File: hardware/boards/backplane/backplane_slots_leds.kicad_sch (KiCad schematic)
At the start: 18 parts, among them J1 DC_IN_SCREW_TERMINAL, J10 I2C_CHAIN_IN, J11 I2C_CHAIN_OUT, J12 LED_EXT_OUT, J2 XT30U(2+2)-F.G.B_SLOT1, J3 XT30U(2+2)-F.G.B_SLOT2, J4 XT30U(2+2)-F.G.B_SLOT3, J5 XT30U(2+2)-F.G.B_SLOT4, J6 XT30U(2+2)-F.G.B_SLOT5, J7 XT30U(2+2)-F.G.B_SLOT6, J8 LED_EXT_IN, J9 DC_CHAIN_OUT

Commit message: Rename XT30U footprint
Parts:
- J2, J3, J4, J5, J6, J7: footprint mini-rack-power:Amass_XT30U_2plus2_F_RightAngle_Mechanical -> mini-rack-power:Amass_XT30U_2plus2_F
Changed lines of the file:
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@@
 			)
 		)
-		(property "Footprint" "mini-rack-power:Amass_XT30U_2plus2_F_RightAngle_Mechanical"
+		(property "Footprint" "mini-rack-power:Amass_XT30U_2plus2_F"
 			(at 92.71 33.02 0)
 			(hide yes)
@@
 			)
 		)
-		(property "Description" "Amass XT30U 2+2 female slot connector; female PCB land pattern needs verification"
+		(property "Description" "Amass XT30U 2+2 female vertical/180-degree slot connector"
 			(at 92.71 33.02 0)
 			(hide yes)
@@
 			)
 		)
-		(property "Footprint" "mini-rack-power:Amass_XT30U_2plus2_F_RightAngle_Mechanical"
+		(property "Footprint" "mini-rack-power:Amass_XT30U_2plus2_F"
 			(at 92.71 55.88 0)
 			(hide yes)
@@
 			)
 		)
-		(property "Description" "Amass XT30U 2+2 female slot connector; female PCB land pattern needs verification"
+		(property "Description" "Amass XT30U 2+2 female vertical/180-degree slot connector"
 			(at 92.71 55.88 0)
 			(hide yes)
@@
 			)
 		)
-		(property "Footprint" "mini-rack-power:Amass_XT30U_2plus2_F_RightAngle_Mechanical"
+		(property "Footprint" "mini-rack-power:Amass_XT30U_2plus2_F"
 			(at 92.71 78.74 0)
 			(hide yes)
@@
 			)
 		)
-		(property "Description" "Amass XT30U 2+2 female slot connector; female PCB land pattern needs verification"
+		(property "Description" "Amass XT30U 2+2 female vertical/180-degree slot connector"
 			(at 92.71 78.74 0)
 			(hide yes)
@@
 			)
 		)
-		(property "Footprint" "mini-rack-power:Amass_XT30U_2plus2_F_RightAngle_Mechanical"
+		(property "Footprint" "mini-rack-power:Amass_XT30U_2plus2_F"
 			(at 151.13 33.02 0)
 			(hide yes)
@@
 			)
 		)
-		(property "Description" "Amass XT30U 2+2 female slot connector; female PCB land pattern needs verification"
+		(property "Description" "Amass XT30U 2+2 female vertical/180-degree slot connector"
 			(at 151.13 33.02 0)
 			(hide yes)
@@
 			)
 		)
-		(property "Footprint" "mini-rack-power:Amass_XT30U_2plus2_F_RightAngle_Mechanical"
+		(property "Footprint" "mini-rack-power:Amass_XT30U_2plus2_F"
 			(at 151.13 55.88 0)
 			(hide yes)
@@
 			)
 		)
-		(property "Description" "Amass XT30U 2+2 female slot connector; female PCB land pattern needs verification"
+		(property "Description" "Amass XT30U 2+2 female vertical/180-degree slot connector"
 			(at 151.13 55.88 0)
 			(hide yes)
@@
 			)
 		)
-		(property "Footprint" "mini-rack-power:Amass_XT30U_2plus2_F_RightAngle_Mechanical"
+		(property "Footprint" "mini-rack-power:Amass_XT30U_2plus2_F"
 			(at 151.13 78.74 0)
 			(hide yes)
@@
 			)
 		)
-		(property "Description" "Amass XT30U 2+2 female slot connector; female PCB land pattern needs verification"
+		(property "Description" "Amass XT30U 2+2 female vertical/180-degree slot connector"
 			(at 151.13 78.74 0)
 			(hide yes)

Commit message: Update board layouts and add SW3538 datasheet
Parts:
- added J14: LED_EXT_IN, Connector_PinHeader_2.54mm:PinHeader_1x03_P2.54mm_Vertical, symbol Connector_Generic:Conn_01x03
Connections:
- net DC_IN+: now also J1.2 (Pin_2); no longer J1.1 (Pin_1)
- net GND: now also J1.1 (Pin_1), J8.1 (Pin_1); no longer D2.3 (VSS), D3.3 (VSS), D4.3 (VSS), D5.3 (VSS), D6.3 (VSS), J1.2 (Pin_2), J8.3 (Pin_3)
- net I2C_UP_SCL: now also J10.2 (Pin_2), J11.2 (Pin_2); no longer J10.3 (Pin_3), J11.3 (Pin_3)
- net I2C_UP_SDA: now also J10.3 (Pin_3), J11.3 (Pin_3); no longer J10.2 (Pin_2), J11.2 (Pin_2)
- net LED_VDD: no longer J8.1 (Pin_1)
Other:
- moved on the sheet: D1, D2, D3, D4, D5, D6, J1, J10, J11, J8

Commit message: Starrting to move things around
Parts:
- removed J2: XT30U(2+2)-F.G.B_SLOT1, mini-rack-power:Amass_XT30U_2plus2_F, symbol Connector_Generic:Conn_01x04
- removed J3: XT30U(2+2)-F.G.B_SLOT2, mini-rack-power:Amass_XT30U_2plus2_F, symbol Connector_Generic:Conn_01x04
- removed J4: XT30U(2+2)-F.G.B_SLOT3, mini-rack-power:Amass_XT30U_2plus2_F, symbol Connector_Generic:Conn_01x04
- removed J5: XT30U(2+2)-F.G.B_SLOT4, mini-rack-power:Amass_XT30U_2plus2_F, symbol Connector_Generic:Conn_01x04
- removed J6: XT30U(2+2)-F.G.B_SLOT5, mini-rack-power:Amass_XT30U_2plus2_F, symbol Connector_Generic:Conn_01x04
- removed J7: XT30U(2+2)-F.G.B_SLOT6, mini-rack-power:Amass_XT30U_2plus2_F, symbol Connector_Generic:Conn_01x04
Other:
- note removed: "XT30 pin assumption: 1=DC_IN+, 2=GND, 3=SDA, 4=SCL. Verify XT30U female electrical footprint before PCB layout."

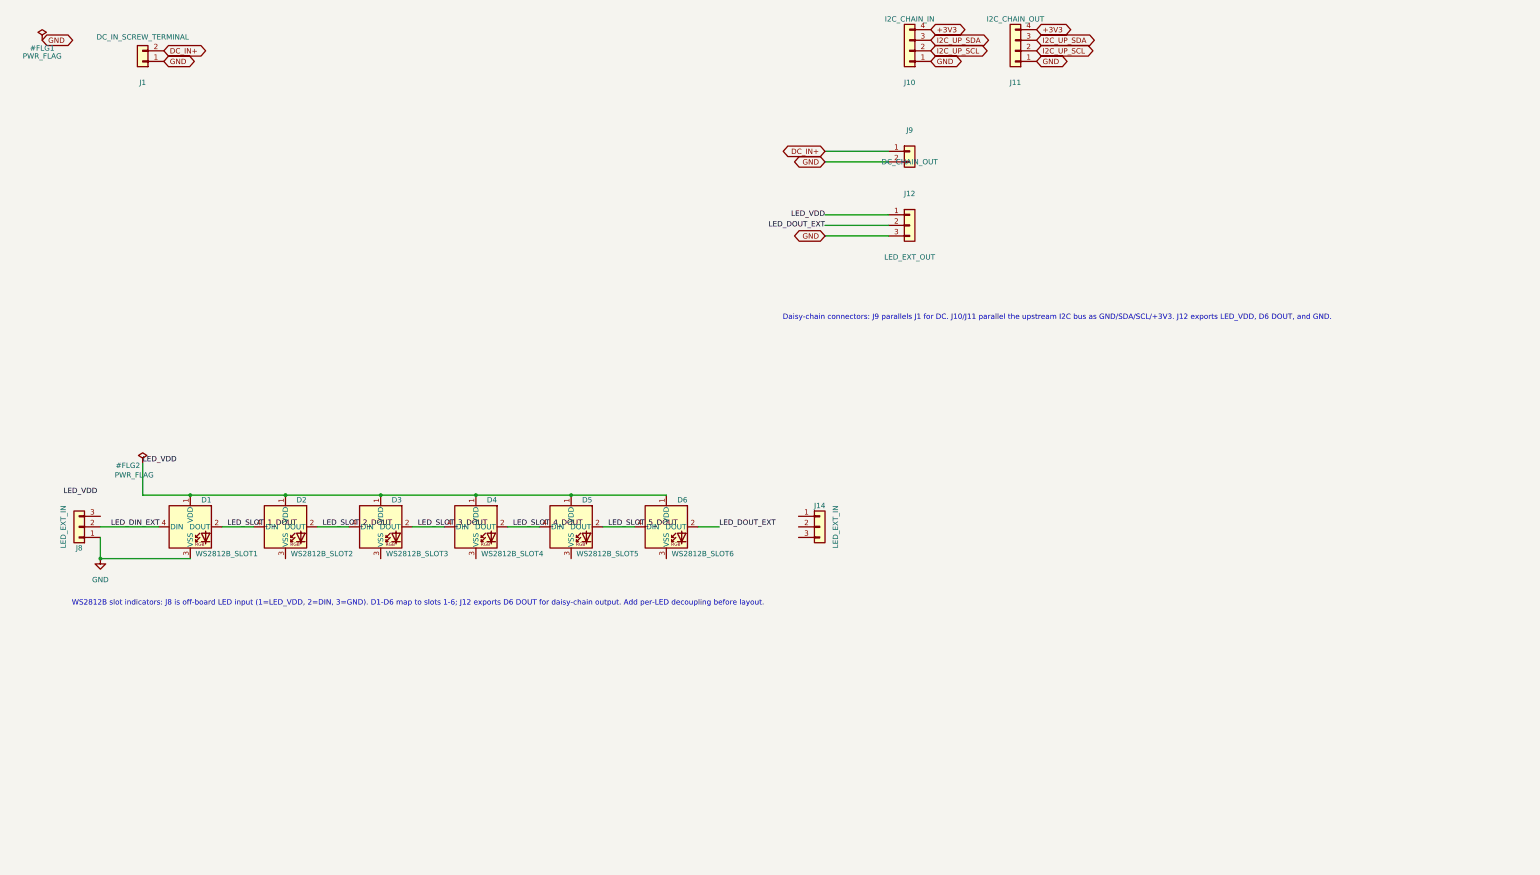
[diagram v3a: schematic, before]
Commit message: Clean up the backplane schematic
And start over with the PCB using a bit saner layout
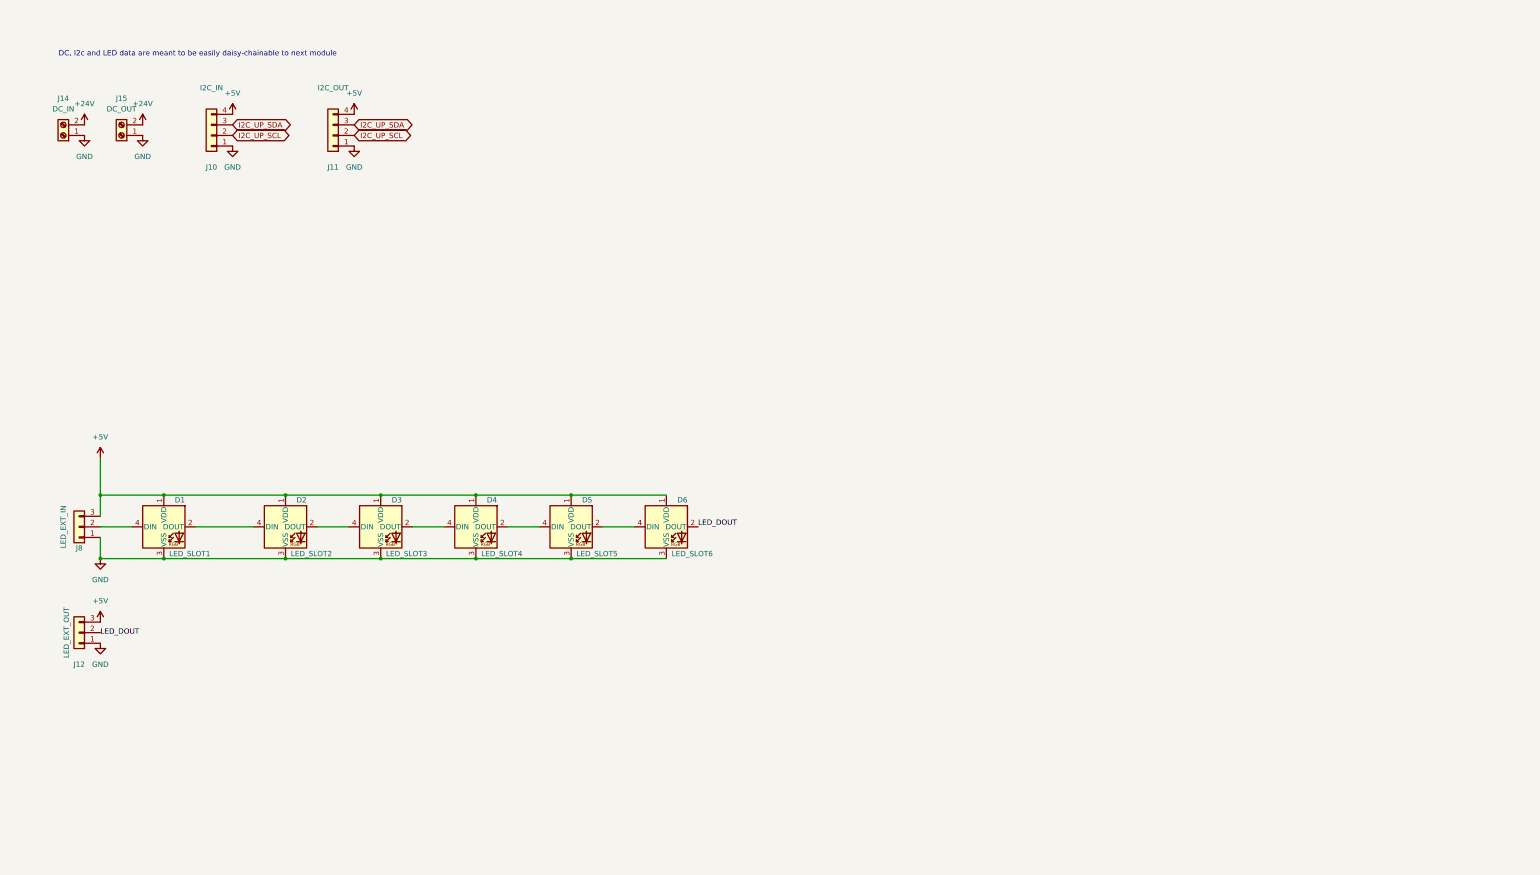
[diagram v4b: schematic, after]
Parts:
- removed J1: DC_IN_SCREW_TERMINAL, TerminalBlock_Phoenix:TerminalBlock_Phoenix_MKDS-1,5-2-5.08_1x02_P5.08mm_Horizontal, symbol Connector_Generic:Conn_01x02
- removed J14: LED_EXT_IN, Connector_PinHeader_2.54mm:PinHeader_1x03_P2.54mm_Vertical, symbol Connector_Generic:Conn_01x03
- removed J9: DC_CHAIN_OUT, TerminalBlock_Phoenix:TerminalBlock_Phoenix_MKDS-1,5-2-5.08_1x02_P5.08mm_Horizontal, symbol Connector_Generic:Conn_01x02
- added J14: DC_IN, symbol Connector:Screw_Terminal_01x02
- added J15: DC_OUT, symbol Connector:Screw_Terminal_01x02
- D1: value WS2812B_SLOT1 -> LED_SLOT1
- D2: value WS2812B_SLOT2 -> LED_SLOT2
- D3: value WS2812B_SLOT3 -> LED_SLOT3
- D4: value WS2812B_SLOT4 -> LED_SLOT4
- D5: value WS2812B_SLOT5 -> LED_SLOT5
- D6: value WS2812B_SLOT6 -> LED_SLOT6
- J10: value I2C_CHAIN_IN -> I2C_IN
- J11: value I2C_CHAIN_OUT -> I2C_OUT
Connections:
- net +3V3 is gone; now on net +5V: J10.4 (Pin_4), J11.4 (Pin_4)
- net GND: now also D2.3 (VSS), D3.3 (VSS), D4.3 (VSS), D5.3 (VSS), D6.3 (VSS), J12.1 (Pin_1), J14.1 (Pin_1), J15.1 (Pin_1); no longer J12.3 (Pin_3)
- net +5V: now reaches J8.3 (Pin_3)
- net +5V: now also D1.1 (VDD), D2.1 (VDD), D3.1 (VDD), D4.1 (VDD), D5.1 (VDD), D6.1 (VDD), J12.3 (Pin_3)
- net LED_DIN_EXT: no longer names the net of D1.4 (DIN), J8.2 (Pin_2)
- net LED_DOUT_EXT renamed LED_DOUT
- net LED_SLOT_1_DOUT: no longer names the net of D1.2 (DOUT), D2.4 (DIN)
- net LED_SLOT_2_DOUT: no longer names the net of D2.2 (DOUT), D3.4 (DIN)
- net LED_SLOT_3_DOUT: no longer names the net of D3.2 (DOUT), D4.4 (DIN)
- net LED_SLOT_4_DOUT: no longer names the net of D4.2 (DOUT), D5.4 (DIN)
- net LED_SLOT_5_DOUT: no longer names the net of D5.2 (DOUT), D6.4 (DIN)
- removed net LED_VDD: D1.1 (VDD), D2.1 (VDD), D3.1 (VDD), D4.1 (VDD), D5.1 (VDD), D6.1 (VDD), J12.1 (Pin_1)
- new net +24V: J14.2 (Pin_2), J15.2 (Pin_2)
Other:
- note added: "DC, I2c and LED data are meant to be easily daisy-chainable to next module"
- note removed: "Daisy-chain connectors: J9 parallels J1 for DC. J10/J11 parallel the upstream I2C bus as GND/SDA/SCL/+3V3. J12 exports LED_VDD, D6 DOUT, and GND."
- note removed: "WS2812B slot indicators: J8 is off-board LED input (1=LED_VDD, 2=DIN, 3=GND). D1-D6 map to slots 1-6; J12 exports D6 DOUT for daisy-chain output. Add per-LED decoupling before layout."
- moved on the sheet: D1, J10

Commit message: Small tweaks to PCB/Schematic + 3d models
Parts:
- added H1, H2, H3, H4: MountingHole_Pad, MountingHole:MountingHole_3.2mm_M3_Pad_Via, symbol Mechanical:MountingHole_Pad
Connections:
- net GND: now also H1.1, H2.1, H3.1, H4.1

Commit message: Split controller hardware from backplane
Add the central controller KiCad project for the WT32 and fan circuit, retain the I2C mux on the backplane, and update the system/interface documentation. Use C7519 arrays for interim slot I2C protection and record assembly-part alternatives.
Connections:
- net +5V: no longer J10.4 (Pin_4), J11.4 (Pin_4)
- net LED_DATA_IN: now reaches D1.4 (DIN), J8.2 (Pin_2)
- new net +3V3: J10.4 (Pin_4), J11.4 (Pin_4)
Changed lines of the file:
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@@
 	)
 	(symbol
-		(lib_id "power:+5V")
+		(lib_id "power:+3V3")
 		(at 66.04 36.83 0)
 		(unit 1)
@@
 			)
 		)
-		(property "Value" "+5V"
+		(property "Value" "+3V3"
 			(at 66.04 31.75 0)
 			(show_name no)
@@
 			)
 		)
-		(property "Description" "Power symbol creates a global label with name \"+5V\""
+		(property "Description" "Power symbol creates a global label with name \"+3V3\""
 			(at 66.04 36.83 0)
 			(hide yes)
@@
 	)
 	(symbol
-		(lib_id "power:+5V")
+		(lib_id "power:+3V3")
 		(at 95.25 36.83 0)
 		(unit 1)
@@
 			)
 		)
-		(property "Value" "+5V"
+		(property "Value" "+3V3"
 			(at 95.25 31.75 0)
 			(show_name no)
@@
 			)
 		)
-		(property "Description" "Power symbol creates a global label with name \"+5V\""
+		(property "Description" "Power symbol creates a global label with name \"+3V3\""
 			(at 95.25 36.83 0)
 			(hide yes)
@@
 		)
 	)
+	(label "LED_DATA_IN"
+		(at 34.29 135.89 0)
+		(effects
+			(font
+				(size 1.27 1.27)
+			)
+			(justify left bottom)
+		)
+	)

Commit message: Select high-current backplane terminals
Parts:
- J14, J15: footprint (none) -> mini-rack-power:DEGSON_DG135T-10.16-02P; LCSC (none) -> C708738; MPN (none) -> DG135T-10.16-02P-14-00A(H); Manufacturer (none) -> DEGSON; Part_source (none) -> LCSC,C708738
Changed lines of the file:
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@@
 			)
 		)
-		(property "Footprint" ""
+		(property "Footprint" "mini-rack-power:DEGSON_DG135T-10.16-02P"
 			(at 25.4 41.91 0)
 			(hide yes)
@@
 			)
 		)
-		(property "Datasheet" ""
+		(property "Datasheet" "https://www.degson.com/content/details_552_880568.html?lang=en"
 			(at 25.4 41.91 0)
 			(hide yes)
@@
 			)
 		)
-		(property "Description" "Generic screw terminal, single row, 01x02, script generated (kicad-library-utils/schlib/autogen/connector/)"
+		(property "Description" "DEGSON DG135T-10.16-02P, 2-position M4 screw terminal, 10.16 mm pitch, 52 A UL / 57 A IEC, LCSC C708738"
+			(at 25.4 41.91 0)
+			(hide yes)
+			(show_name no)
+			(do_not_autoplace no)
+			(effects
+				(font
+					(size 1.27 1.27)
+				)
+			)
+		)
+		(property "Manufacturer" "DEGSON"
+			(at 25.4 41.91 0)
+			(hide yes)
+			(show_name no)
+			(do_not_autoplace no)
+			(effects
+				(font
+					(size 1.27 1.27)
+				)
+			)
+		)
+		(property "MPN" "DG135T-10.16-02P-14-00A(H)"
+			(at 25.4 41.91 0)
+			(hide yes)
+			(show_name no)
+			(do_not_autoplace no)
+			(effects
+				(font
+					(size 1.27 1.27)
+				)
+			)
+		)
+		(property "LCSC" "C708738"
+			(at 25.4 41.91 0)
+			(hide yes)
+			(show_name no)
+			(do_not_autoplace no)
+			(effects
+				(font
+					(size 1.27 1.27)
+				)
+			)
+		)
+		(property "Part_source" "LCSC,C708738"
 			(at 25.4 41.91 0)
 			(hide yes)
@@
 			)
 		)
-		(property "Footprint" ""
+		(property "Footprint" "mini-rack-power:DEGSON_DG135T-10.16-02P"
 			(at 39.37 41.91 0)
 			(hide yes)
@@
 			)
 		)
-		(property "Datasheet" ""
+		(property "Datasheet" "https://www.degson.com/content/details_552_880568.html?lang=en"
 			(at 39.37 41.91 0)
 			(hide yes)
@@
 			)
 		)
-		(property "Description" "Generic screw terminal, single row, 01x02, script generated (kicad-library-utils/schlib/autogen/connector/)"
+		(property "Description" "DEGSON DG135T-10.16-02P, 2-position M4 screw terminal, 10.16 mm pitch, 52 A UL / 57 A IEC, LCSC C708738"
 			(at 39.37 41.91 0)
 			(hide yes)
+			(show_name no)
+			(do_not_autoplace no)
+			(effects
+				(font
+					(size 1.27 1.27)
+				)
+			)
+		)
+		(property "Manufacturer" "DEGSON"
+			(at 39.37 41.91 0)
+			(hide yes)
+			(show_name no)
+			(do_not_autoplace no)
+			(effects
+				(font
+					(size 1.27 1.27)
+				)
+			)
+		)
+		(property "MPN" "DG135T-10.16-02P-14-00A(H)"
+			(at 39.37 41.91 0)
+			(hide yes)
+			(show_name no)
+			(do_not_autoplace no)
+			(effects
+				(font
+					(size 1.27 1.27)
+				)
+			)
+		)
+		(property "LCSC" "C708738"
+			(at 39.37 41.91 0)
+			(hide yes)
+			(show_name no)
+			(do_not_autoplace no)
+			(effects
+				(font
+					(size 1.27 1.27)
+				)
+			)
+		)
+		(property "Part_source" "LCSC,C708738"
+			(at 39.37 41.91 0)
+			(hide yes)
